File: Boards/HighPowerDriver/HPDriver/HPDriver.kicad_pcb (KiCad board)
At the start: 4 copper layers, 100.6 x 76.2 mm, 118 parts, among them J1 USB_B_Mini, J2 60V_In, J3 Coils, J4 Screw_Terminal_01x06, J5 AVR-ISP-6, Q1 IRFR5410, Q10 IRF4950S, Q11 BC817, Q12 BC817, Q13 BC817, Q14 BC817, Q2 IRFR3910, Q3 IRFR3910, Q4 IRFR5410, Q5 IRFR5410, Q6 IRFR3910, Q7 IRFR3910, Q8 IRFR5410, Q9 BC817, SW1 SW_Push, U1 LM5009MM, U10 ATtiny2313A-SU, U2 TMC262, U3 FT230XS, U4 SFH6156, U5 SFH6156, U6 TLP118, U7 LTV-827S, U8 LTV-827S, U9 74HC14, X1 16MHz, Y1 20MHz

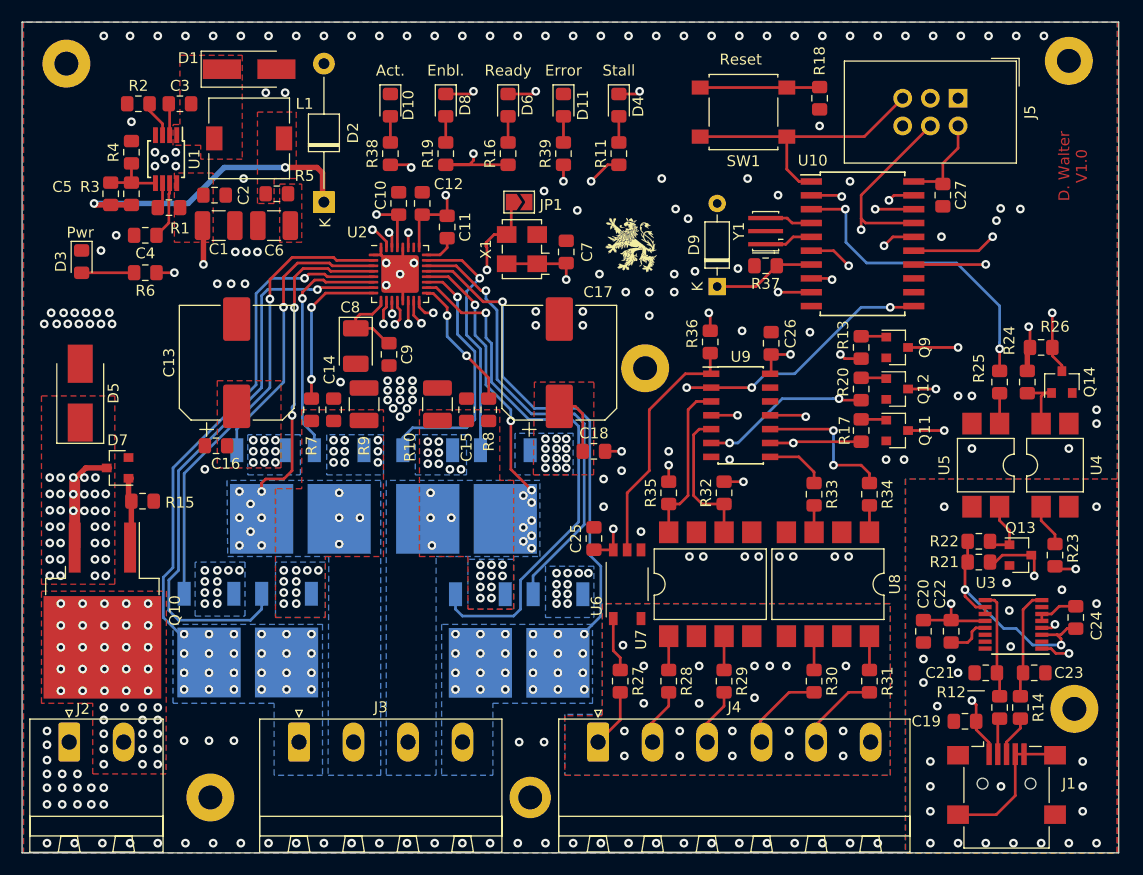
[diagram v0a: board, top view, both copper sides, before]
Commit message: Changed position of LEDs, improved routing
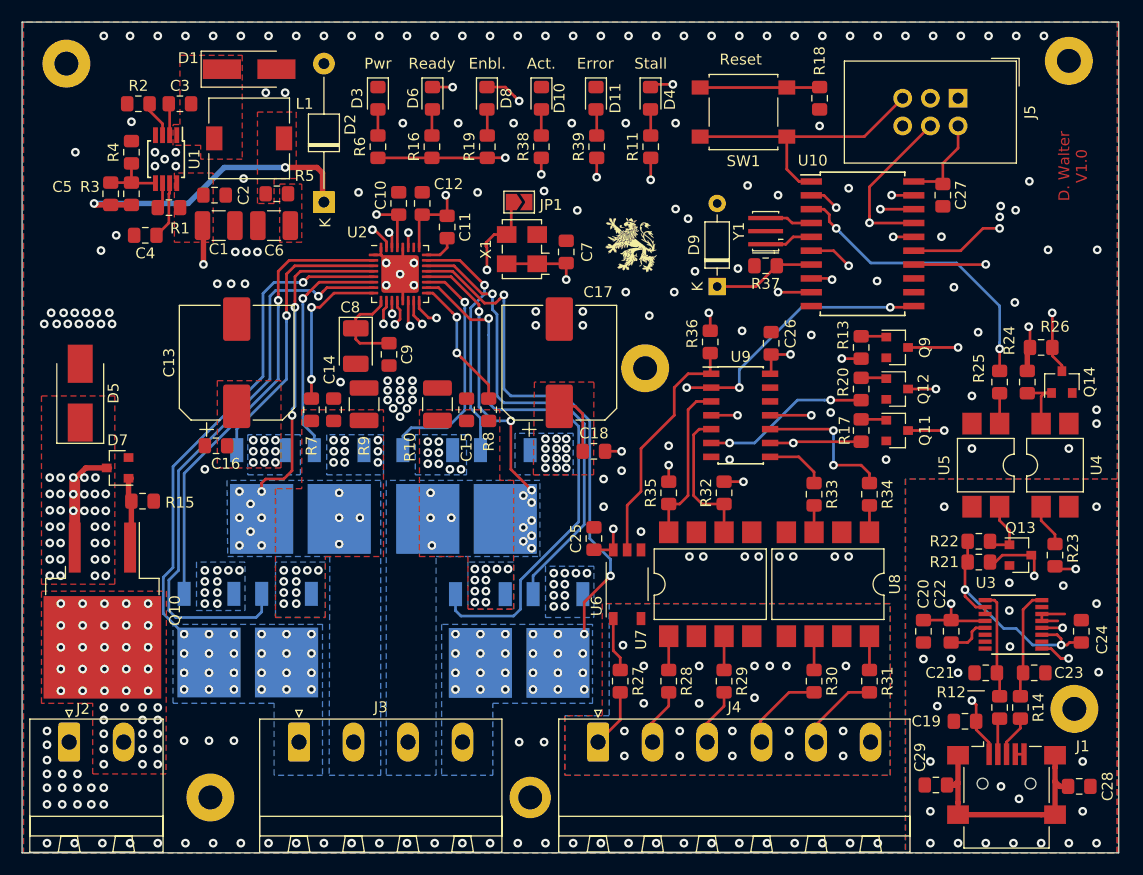
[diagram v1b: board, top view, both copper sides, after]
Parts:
- added C28: 10nF, Capacitor_SMD:C_0805_2012Metric_Pad1.15x1.40mm_HandSolder, F.Cu at (181.3, 134.9)
- added C29: 10nF, Capacitor_SMD:C_0805_2012Metric_Pad1.15x1.40mm_HandSolder, F.Cu at (168.1, 134.7)
- moved D3 31.0 mm to (117.0, 71.8)
- moved R6 24.3 mm to (117.0, 76.2), turned to 90 degrees
- moved D10 13.9 mm to (132.0, 71.8)
- moved R38 13.9 mm to (132.0, 76.2)
- moved R16 7.01 mm to (121.9, 76.2)
- moved D6 6.97 mm to (122.0, 71.8)
- moved R19 3.86 mm to (127.0, 76.2)
- moved D8 3.83 mm to (127.0, 71.8)
- moved R39 3.11 mm to (137.0, 76.2)
- moved D11 3.05 mm to (137.0, 71.8)
- moved R11 2.99 mm to (142.0, 76.2)
- moved D4 2.97 mm to (142.0, 71.8)
- moved C24 1.37 mm to (181.5, 120.7)
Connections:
- J1 pad 6: GNDS -> Net-(C28-Pad1)
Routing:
- net Net-(C28-Pad1): track 0.00 -> 22.4 mm
- net GNDS: track 21.5 -> 9.03 mm, vias 26 -> 25
- net /Connector/Active: track 66.6 -> 55.0 mm
- net Net-(D6-Pad1): track 76.0 -> 83.2 mm
- net Net-(D4-Pad1): track 61.1 -> 57.8 mm
- net Net-(D8-Pad1): track 75.8 -> 72.7 mm
- net /Connector/Rx: track 33.7 -> 36.8 mm
- net /Connector/Error: track 52.7 -> 49.9 mm
- net Net-(D3-Pad2): track 4.82 -> 2.39 mm
- net Net-(Q7-Pad1): track 23.7 -> 22.1 mm
- net /Connector/Coil_B2: track 46.6 -> 48.2 mm, vias 25 -> 26
- net /Connector/Stall: track 77.0 -> 75.4 mm
- net /Connector/Tx: track 29.2 -> 27.8 mm
- net Net-(Q3-Pad1): track 49.5 -> 50.8 mm
- net Net-(Q13-Pad3): track 12.6 -> 13.8 mm
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
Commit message: Layout v1.0 finished
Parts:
- removed the R29 at (148.7, 125.2)
- added D12: LED_Gn, LED_SMD:LED_0805_2012Metric_Pad1.15x1.40mm_HandSolder, F.Cu at (168.8, 113.4)
- added R31: 200R, Resistor_SMD:R_0805_2012Metric_Pad1.15x1.40mm_HandSolder, F.Cu at (148.7, 125.2)
- added R40: R, Resistor_SMD:R_0805_2012Metric_Pad1.15x1.40mm_HandSolder, F.Cu at (130.9, 128.8)
- added R41: R, Resistor_SMD:R_0805_2012Metric_Pad1.15x1.40mm_HandSolder, F.Cu at (97.3, 90.4)
- added R42: 180R, Resistor_SMD:R_0805_2012Metric_Pad1.15x1.40mm_HandSolder, F.Cu at (171.6, 113.4)
- added REF**: ESD-Logo_8.9x8mm_SilkScreen, Symbol:ESD-Logo_8.9x8mm_SilkScreen, F.Cu at (117.5, 121.9)
- added REF**: ESD-Logo_8.9x8mm_SilkScreen, Symbol:ESD-Logo_8.9x8mm_SilkScreen, B.Cu at (99.7, 71.1)
- added TH1: Thermistor_NTC, Resistor_SMD:R_0805_2012Metric_Pad1.15x1.40mm_HandSolder, B.Cu at (130.6, 128.8)
- added TH2: Thermistor_NTC, Resistor_SMD:R_0805_2012Metric_Pad1.15x1.40mm_HandSolder, B.Cu at (101.3, 109.7)
- D2: footprint Diode_THT:D_T-1_P12.70mm_Horizontal -> Diode_SMD:D_SMB
- D9: footprint Diode_THT:D_DO-35_SOD27_P7.62mm_Horizontal -> Diode_SMD:D_SOD-123
- moved C9 5.99 mm to (112.4, 93.1)
- moved D2 5.72 mm to (111.9, 75.6)
- moved R37 3.66 mm to (150.5, 90.2)
- moved Q13 2.79 mm to (178.7, 113.7)
- moved D9 2.79 mm to (150.5, 87.6), turned to 180 degrees
- moved R24 2.54 mm to (181.6, 113.5)
- moved R20 2.54 mm to (174.6, 114.4)
- moved R21 2.54 mm to (174.6, 112.4)
- moved C22 1.40 mm to (168.4, 120.7)
- moved C4 1.30 mm to (96.9, 84.6), turned to 270 degrees
- moved R29 1.02 mm to (140.2, 125.2)
- moved C11 0.90 mm to (123.2, 84.5)
- moved C24 0.89 mm to (170.4, 120.7)
- moved C3 0.76 mm to (98.8, 73.0)
- moved R2 0.76 mm to (95.0, 73.0)
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- renumbered C28 to C19, C29 to C20, C19 to C21, C20 to C22, C21 to C23, C22 to C24, C23 to C25, C24 to C26, C25 to C28, C26 to C29, D7 to D5, D5 to D6, D6 to D7, J2 to J1, J1 to J2, R15 to R12, R12 to R14, R14 to R15, R19 to R18, R20 to R19, R21 to R20, R22 to R21, R18 to R22, R38 to R23, R23 to R24, R39 to R25, R24 to R26, R25 to R27, R26 to R28, R27 to R29, R28 to R30, R30 to R32, R31 to R33, R32 to R34, R33 to R35, R34 to R36, R35 to R38, R36 to R39
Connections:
- C21 pad 1: Net-(C19-Pad1) (its old number) -> +5VP
- C22 pad 1: Net-(C19-Pad1) (its old number) -> +5VP
- C24 pad 1: Net-(C19-Pad1) (its old number) -> +5VP
- J2 pad 1: Net-(C19-Pad1) (its old number) -> +5VP
- R35 pad 1: Net-(R33-Pad1) (its old number) -> Net-(R35-Pad1)
- R36 pad 1: Net-(R34-Pad1) (its old number) -> Net-(R36-Pad1)
- U10 pad 12: Net-(U10-Pad12) -> /Controller/Temp1
- U10 pad 13: Net-(U10-Pad13) -> /Controller/Temp2
- U3 pad 12: Net-(C19-Pad1) (its old number) -> +5VP
- U9 pad 10: Net-(R34-Pad1) (its old number) -> Net-(R35-Pad1)
- U9 pad 8: Net-(R33-Pad1) (its old number) -> Net-(R36-Pad1)
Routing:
- net /Controller/Temp1: track 0.00 -> 104.1 mm, vias 0 -> 4
- net /Controller/Temp2: track 0.00 -> 82.0 mm, vias 0 -> 2
- net +5VP: track 0.00 -> 24.8 mm, vias 0 -> 2
- net Net-(C19-Pad1) (its old number): track 22.5 -> 0.00 mm, vias 2 -> 0
- net +5V: track 79.9 -> 94.8 mm, vias 12 -> 15
- net Net-(R34-Pad1) (its old number): track 13.5 -> 0.00 mm, vias 2 -> 0
- net Net-(D12-Pad1): track 0.00 -> 11.8 mm, vias 0 -> 2
- net Net-(R36-Pad1): track 0.00 -> 10.6 mm
- net Net-(R35-Pad1): track 0.00 -> 8.45 mm, vias 0 -> 2
- net Net-(R33-Pad1) (its old number): track 5.62 -> 0.00 mm
- net /Driver/DriveEN: track 71.0 -> 66.0 mm
- net +48V: track 80.2 -> 84.6 mm, vias 76 -> 72
- net Net-(C3-Pad2): track 0.00 -> 3.57 mm
- net Net-(R24-Pad2): track 13.3 -> 10.5 mm
- net Net-(J1-Pad2): track 0.00 -> 2.79 mm, vias 41 -> 23
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- removed copper zone on In1.Cu, net GNDA
- removed copper zone on In2.Cu, net GNDA
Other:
- board text added: "12- 60V"
- board text added: "Dir <"
- board text added: "Enbl<"
- board text added: "GND"
- board text added: "Heatsink required!"
- board text added: "Isolated"
- board text added: "M_A1"
- board text added: "M_A2"
- board text added: "M_B1"
- board text added: "M_B2"
- board text added: "Rdy >"
- board text added: "Stall>"
- board text added: "Step<"
- board text added: "USB Isolated"

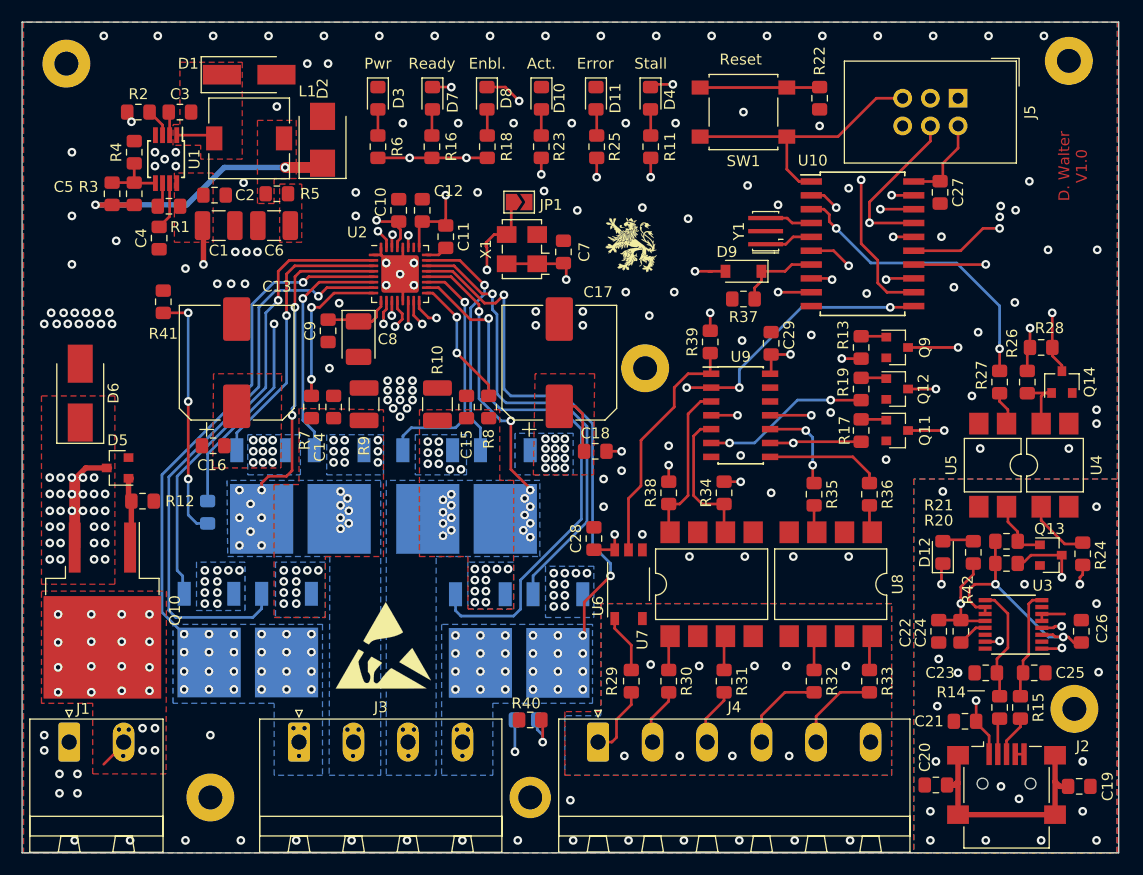
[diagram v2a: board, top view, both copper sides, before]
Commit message: Added Control Logic for Enable/Step/Dir Signals
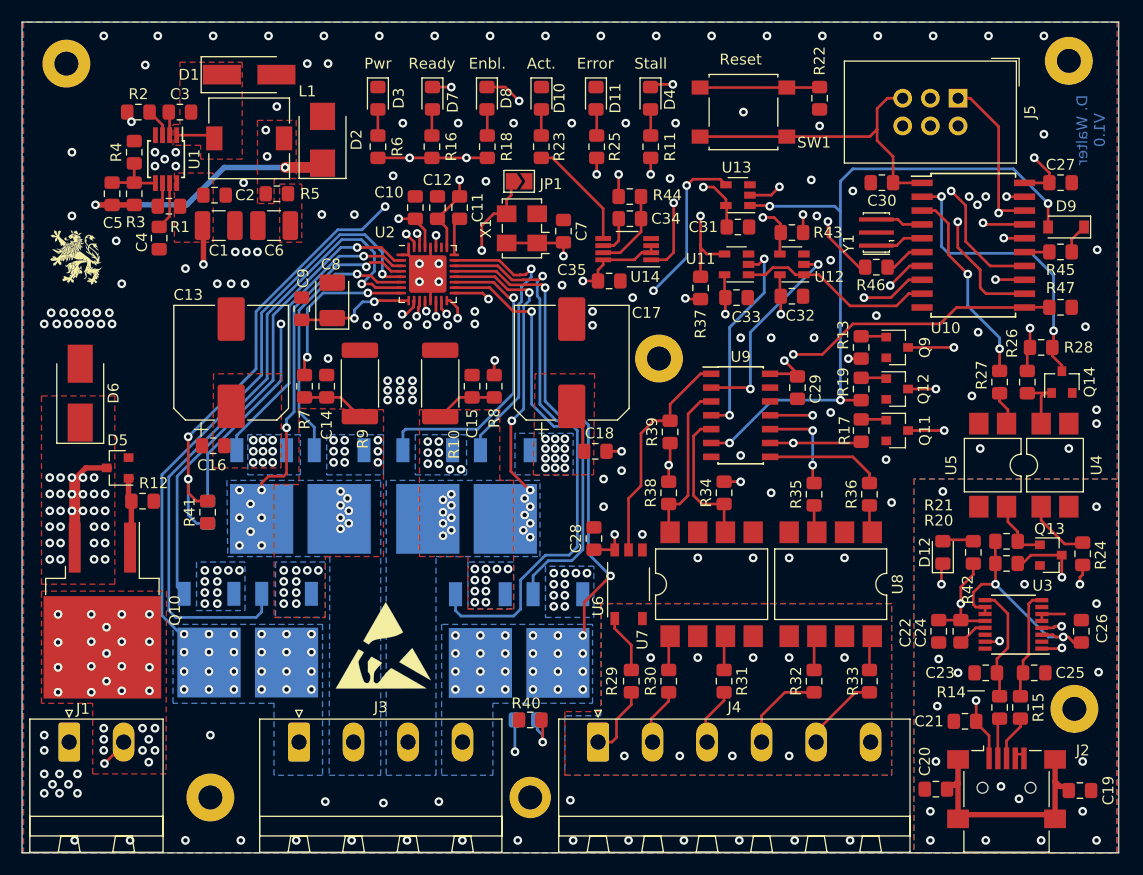
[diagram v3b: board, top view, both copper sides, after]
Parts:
- added C30: 100nF, Capacitor_SMD:C_0805_2012Metric_Pad1.15x1.40mm_HandSolder, F.Cu at (163.2, 79.5)
- added C31: 100nF, Capacitor_SMD:C_0805_2012Metric_Pad1.15x1.40mm_HandSolder, F.Cu at (150.0, 83.6)
- added C32: 100nF, Capacitor_SMD:C_0805_2012Metric_Pad1.15x1.40mm_HandSolder, F.Cu at (154.9, 89.9)
- added C33: 100nF, Capacitor_SMD:C_0805_2012Metric_Pad1.15x1.40mm_HandSolder, F.Cu at (149.9, 90.0)
- added C34: 1µF, Capacitor_SMD:C_0805_2012Metric_Pad1.15x1.40mm_HandSolder, F.Cu at (140.1, 82.8)
- added C35: 100nF, Capacitor_SMD:C_0805_2012Metric_Pad1.15x1.40mm_HandSolder, F.Cu at (138.2, 88.5)
- added R43: 270R, Resistor_SMD:R_0805_2012Metric_Pad1.15x1.40mm_HandSolder, F.Cu at (154.9, 84.1)
- added R44: 100k, Resistor_SMD:R_0805_2012Metric_Pad1.15x1.40mm_HandSolder, F.Cu at (140.1, 80.8)
- added R45: 270R, Resistor_SMD:R_0805_2012Metric_Pad1.15x1.40mm_HandSolder, F.Cu at (179.6, 85.9)
- added R46: 270R, Resistor_SMD:R_0805_2012Metric_Pad1.15x1.40mm_HandSolder, F.Cu at (162.7, 87.2)
- added R47: 10k, Resistor_SMD:R_0805_2012Metric_Pad1.15x1.40mm_HandSolder, F.Cu at (179.6, 90.9)
- added U11: 74LVC1G125, Package_TO_SOT_SMD:SOT-23-5, F.Cu at (149.9, 87.0)
- added U12: 74LVC1G125, Package_TO_SOT_SMD:SOT-23-5, F.Cu at (154.9, 87.0)
- added U13: 74AHC1G00, Package_TO_SOT_SMD:SOT-23-5, F.Cu at (150.0, 80.6)
- added U14: 74LVC1G123, Package_SO:VSSOP-8_3.0x3.0mm_P0.65mm, F.Cu at (139.8, 85.6)
- D9: value 1N4148 -> D
- R10, R9: value 20mR -> 25mR; footprint Resistor_SMD:R_1210_3225Metric_Pad1.42x2.65mm_HandSolder -> Resistor_SMD:R_2512_6332Metric_Pad1.40x3.35mm_HandSolder
- R25: value 180R -> 220R
- R37: value 10k -> 270R
- moved G*** 50.9 mm to (89.3, 86.4)
- moved D9 29.9 mm to (180.1, 83.6)
- moved R41 19.7 mm to (101.3, 109.7), turned to 270 degrees
- moved C27 11.1 mm to (179.6, 79.5), turned to 0 degrees
- moved Y1 10.2 mm to (162.7, 84.1)
- moved U10 10.2 mm to (171.6, 85.2)
- moved R39 9.04 mm to (143.8, 102.4), turned to 270 degrees
- moved C29 4.73 mm to (155.4, 98.3), turned to 270 degrees
- moved C8 4.30 mm to (112.8, 90.3), turned to 90 degrees
- moved R37 4.07 mm to (146.6, 89.2), turned to 270 degrees
- moved C9 3.15 mm to (110.0, 91.1), turned to 90 degrees
- moved C11 2.95 mm to (124.5, 81.8)
- moved U2 2.54 mm to (121.5, 87.9)
- moved C14 2.01 mm to (112.3, 98.2)
- moved R7 2.01 mm to (110.2, 98.2)
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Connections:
- D9 pad 2: /Driver/DriveEN -> /Connector/Enable
- R19 pad 1: /Driver/DriveEN -> /Connector/Enable
- R37 pad 1: Net-(D9-Pad1) -> /Driver/Dir
- R37 pad 2: GND -> Net-(R37-Pad2)
- U10 pad 11: /Connector/Step -> /Connector/Ready
- U10 pad 15: /Connector/Active -> Net-(R45-Pad2)
- U10 pad 6: /Connector/Stall -> Net-(R46-Pad2)
- U10 pad 7: Net-(D9-Pad1) -> Net-(R43-Pad2)
- U10 pad 8: /Connector/Ready -> Net-(R37-Pad2)
- U10 pad 9: /Connector/Dir -> /Controller/Local_Ctrl
- U2 pad 26: Net-(U2-Pad26) -> (no net)
- U2 pad 30: /Connector/Dir -> /Driver/Dir
- U2 pad 31: /Connector/Step -> /Driver/Step
- U3 pad 14: Net-(U3-Pad14) -> (no net)
- U3 pad 16: Net-(U3-Pad16) -> (no net)
- U3 pad 2: Net-(U3-Pad2) -> (no net)
- U3 pad 7: Net-(U3-Pad7) -> (no net)
- U9 pad 12: Net-(U9-Pad12) -> (no net)
- U9 pad 13: Net-(U9-Pad13) -> (no net)
- U9 pad 6: /Driver/DriveEN -> /Connector/Enable
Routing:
- net /Connector/Enable: track 0.00 -> 67.0 mm, vias 0 -> 4
- net /Connector/Step: track 71.8 -> 19.0 mm, vias 5 -> 2
- net /Driver/Step: track 0.00 -> 47.7 mm, vias 0 -> 3
- net /Connector/Dir: track 64.4 -> 19.0 mm, vias 4 -> 2
- net /Connector/Active: track 55.1 -> 10.3 mm, vias 2 -> 0
- net /Driver/Dir: track 0.00 -> 36.7 mm, vias 0 -> 2
- net /Connector/Ready: track 26.8 -> 60.7 mm, vias 2 -> 3
- net Net-(R37-Pad2): track 0.00 -> 24.1 mm, vias 0 -> 2
- net /Driver/DriveEN: track 66.0 -> 44.4 mm, vias 4 -> 3
- net +5V: track 94.8 -> 115.4 mm, vias 15 -> 22
- net Net-(R43-Pad2): track 0.00 -> 19.6 mm, vias 0 -> 2
- net /Controller/Local_Ctrl: track 0.00 -> 18.1 mm
- net /Controller/SCK: track 67.4 -> 78.6 mm
- net /Controller/MOSI: track 67.1 -> 77.7 mm
- net /Controller/MISO: track 68.2 -> 78.2 mm
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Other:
- rule pad_to_mask_clearance: 0.051 -> 0

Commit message: Layout optimizations
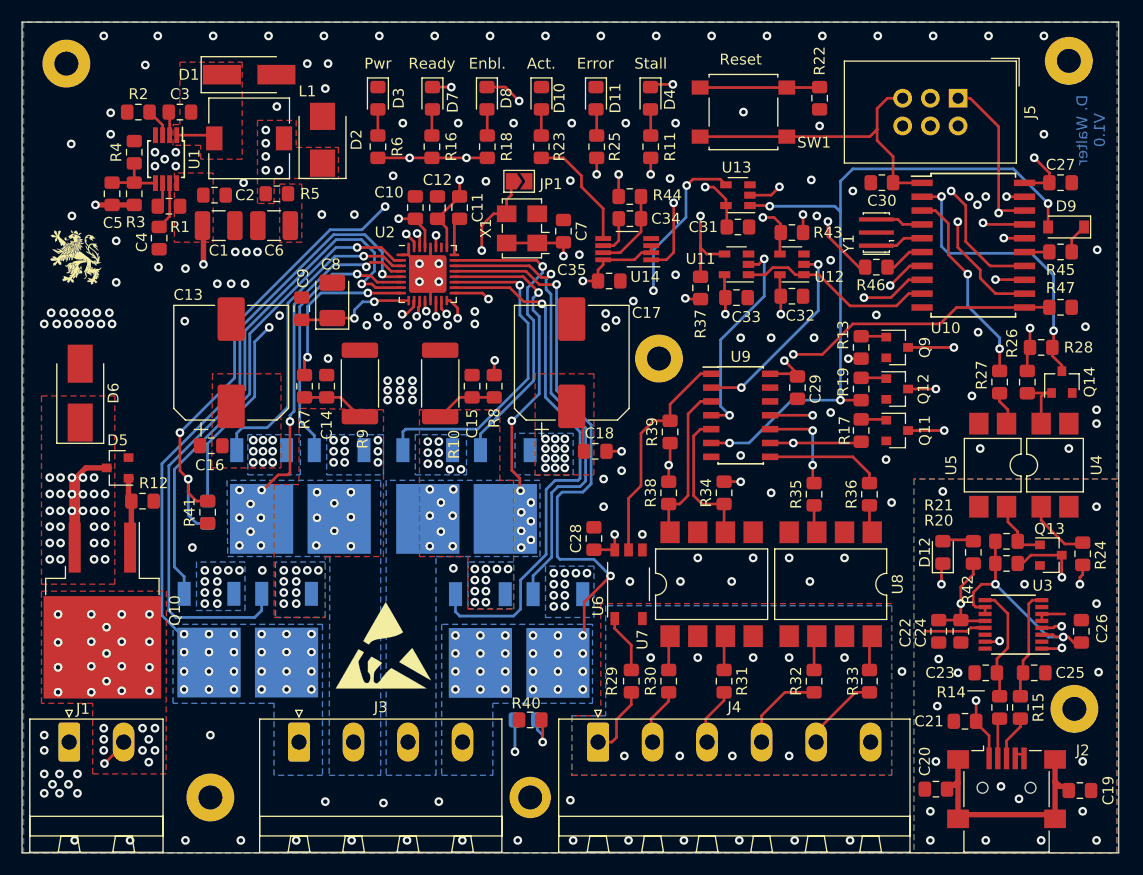
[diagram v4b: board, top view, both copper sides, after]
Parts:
- moved C16 0.18 mm to (101.7, 103.6)
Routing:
- net +5V: track 115.4 -> 92.8 mm, vias 22 -> 24
- net /Connector/Coil_B2: track 45.8 -> 51.0 mm
- net GNDS: track 6.32 -> 10.1 mm
- net Net-(Q7-Pad1): track 28.1 -> 30.2 mm
- net Net-(Q8-Pad1): track 26.4 -> 28.0 mm
- net Net-(Q1-Pad1): track 27.7 -> 29.3 mm
- net /Connector/Coil_B1: track 27.2 -> 28.3 mm
- net /Controller/Temp1: track 107.0 -> 108.0 mm
- net /Connector/Dir: track 19.0 -> 19.7 mm
- net /Connector/Step: track 19.0 -> 18.3 mm
- net /Driver/DriveEN: track 44.4 -> 45.0 mm
- net /Connector/Active: track 10.3 -> 10.9 mm
- net /Connector/Coil_A2: track 30.9 -> 30.8 mm, vias 17 -> 18
- net GND: vias 153 -> 169
- added copper zone on In2.Cu, net GNDA
